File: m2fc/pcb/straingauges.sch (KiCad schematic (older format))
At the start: 29 parts

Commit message: update more bits on flight computer..
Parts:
- removed IC?: OP1177, 8MSOP, symbol OP1177
- removed IC? (x2): OP2177, symbol OP2177
- added IC?: AD8541, SC-70-5, symbol AD8541
- added IC? (x2): AD8656, SOIC8, symbol AD8656
- added TP? (x3): TESTPAD, symbol TESTPAD
- C?: value 1n -> 10n; footprint (none) -> 0603; Farnell (none) -> 2112704
- C? (x2): value C -> 8.2n; footprint (none) -> 0603; Farnell (none) -> 2210859
- C? (x2): value C -> 82n; footprint (none) -> 0603; Farnell (none) -> 1865539
- R?: Farnell 1160313 -> 2116614
- R?: value 10k -> 1k; Farnell 2332016 -> 2116678
- R?: value R -> 1.69k; footprint (none) -> 0603; Farnell (none) -> 2116702
- R?: value R -> 6.04k; footprint (none) -> 0603; Farnell (none) -> 2116761
- R?: value R -> 562; footprint (none) -> 0603; Farnell (none) -> 2117134
- R?: value R -> 17.8k; footprint (none) -> 0603; Farnell (none) -> 2117295
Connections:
- net labels added: VCC_2_REF
- wire segments 90 -> 102
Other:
- note added: "FILTERING\n==================\nSignals of interest: 0 to 1200Hz\nNyquist: 10kHz\nSample: 20kHz\n\nFRONTEND FILTER\n------------------\nFc = 1/(2 pi RC) = 16kHz\n\nANTIALIAS FILTER\n------------------\n-3dB: 2kHz\nRejection at Nyquist: -55dB"
- note added: "STRAIN GAUGES"
- note removed: "FILTERING\n===============\nSignals of interest: 0 to 1kHz\nNyquist: 5kHz\nSample: 10kHz\n\nFRONTEND FILTER\n------------------\nFc = 1/(2 pi RC) = 15915Hz\n\nANTIALIAS FILTER\n------------------\nFc = 2000Hz\nRejection at Nyquist:"
- moved on the sheet: C?, IC?, K?, R?

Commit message: everything... wired... up...
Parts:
- removed C? (x4): 10µ, 1411, symbol CP1
- removed C? (x4): 100n, 0603, symbol C
- removed C?: 10n, 0603, symbol C
- removed C? (x2): 8.2n, 0603, symbol C
- removed C? (x2): 82n, 0603, symbol C
- removed IC?: AD8226, 8MSOP, symbol AD8226
- removed IC?: AD8541, SC-70-5, symbol AD8541
- removed IC? (x2): AD8656, SOIC8, symbol AD8656
- removed K?: CONN_3, symbol CONN_3
- removed R?: 249, 0603, symbol R
- removed R? (x2): 10k, 0603, symbol R
- removed R? (x3): 120, 0603, symbol R
- removed R?: 1k, 0603, symbol R
- removed R?: 1.69k, 0603, symbol R
- removed R?: 6.04k, 0603, symbol R
- removed R?: 562, 0603, symbol R
- removed R?: 17.8k, 0603, symbol R
- removed TP? (x3): TESTPAD, symbol TESTPAD
- added C? (x12): 100n, 0603, symbol C
- added C? (x12): 10µ, 1411, symbol CP1
- added C? (x3): 10n, 0603, symbol C
- added C? (x6): 8.2n, 0603, symbol C
- added C? (x6): 82n, 0603, symbol C
- added IC? (x3): AD8226, 8MSOP, symbol AD8226
- added IC? (x3): AD8541, SC-70-5, symbol AD8541
- added IC? (x6): AD8656, SOIC8, symbol AD8656
- added K? (x3): CONN_3, symbol CONN_3
- added R? (x6): 10k 0.1%, 0603, symbol R
- added R? (x3): 249, 0603, symbol R
- added R? (x3): 1k, 0603, symbol R
- added R? (x3): 1.69k, 0603, symbol R
- added R? (x3): 6.04k, 0603, symbol R
- added R? (x3): 562, 0603, symbol R
- added R? (x3): 17.8k, 0603, symbol R
- added TP? (x3): TESTPAD, symbol TESTPAD
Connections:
- net labels added: STRAIN_2, STRAIN_3
- net labels removed: VCC_2_REF
- wire segments 102 -> 225
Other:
- note added: "STRAIN GAUGE 2"
- note added: "STRAIN GAUGE 3"

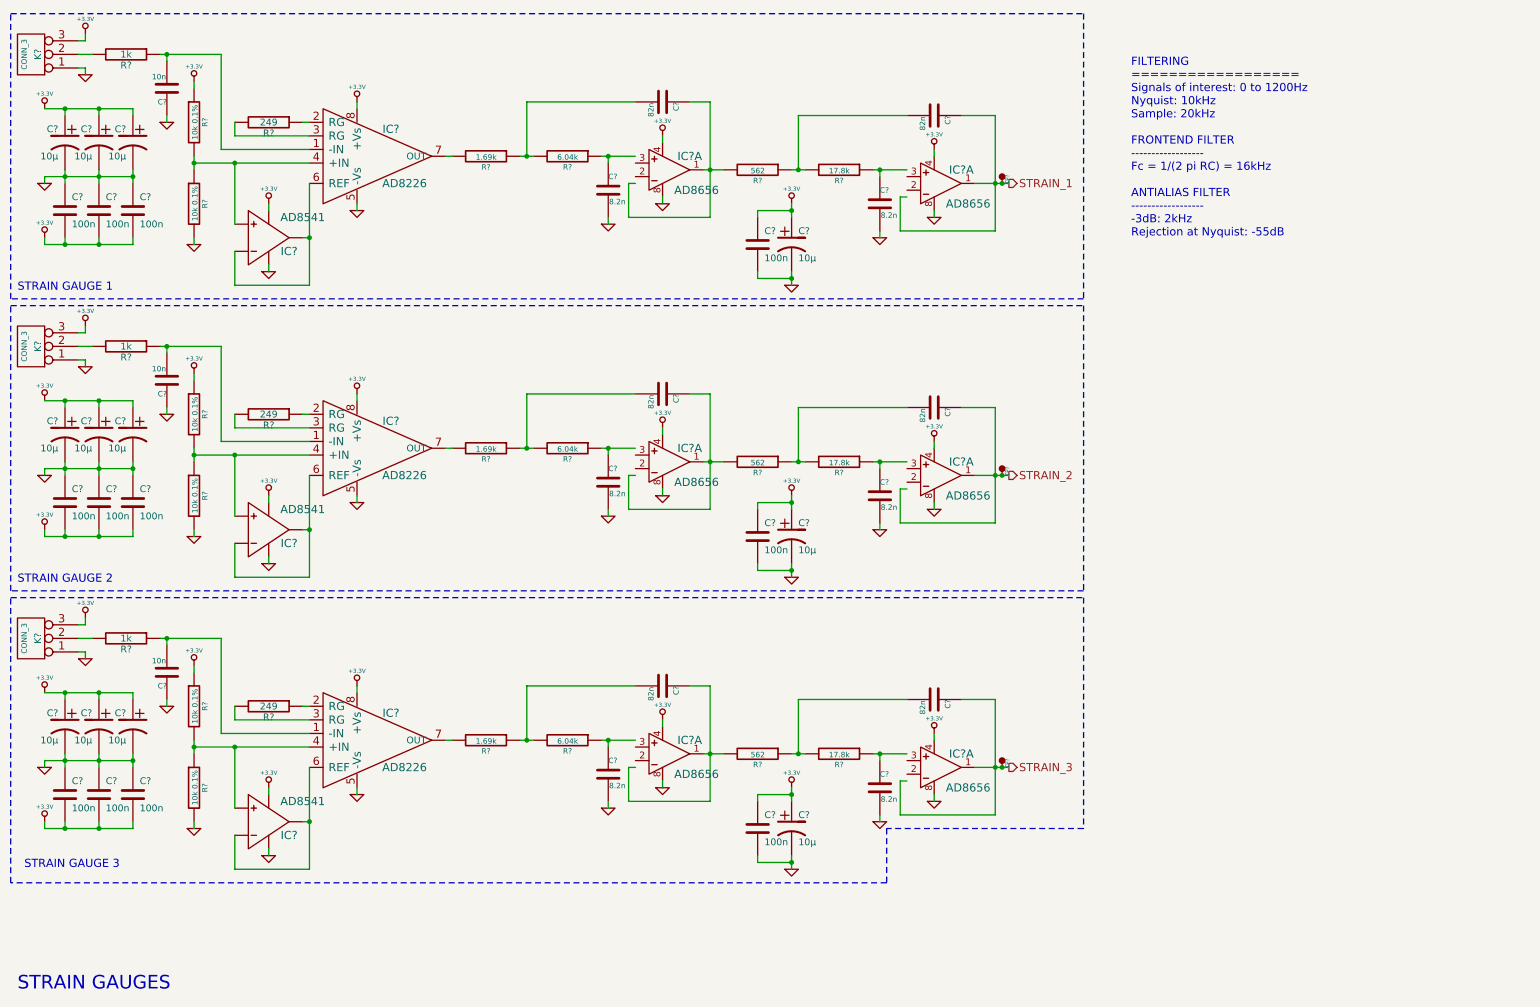
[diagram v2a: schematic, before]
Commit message: fix all the erc errors
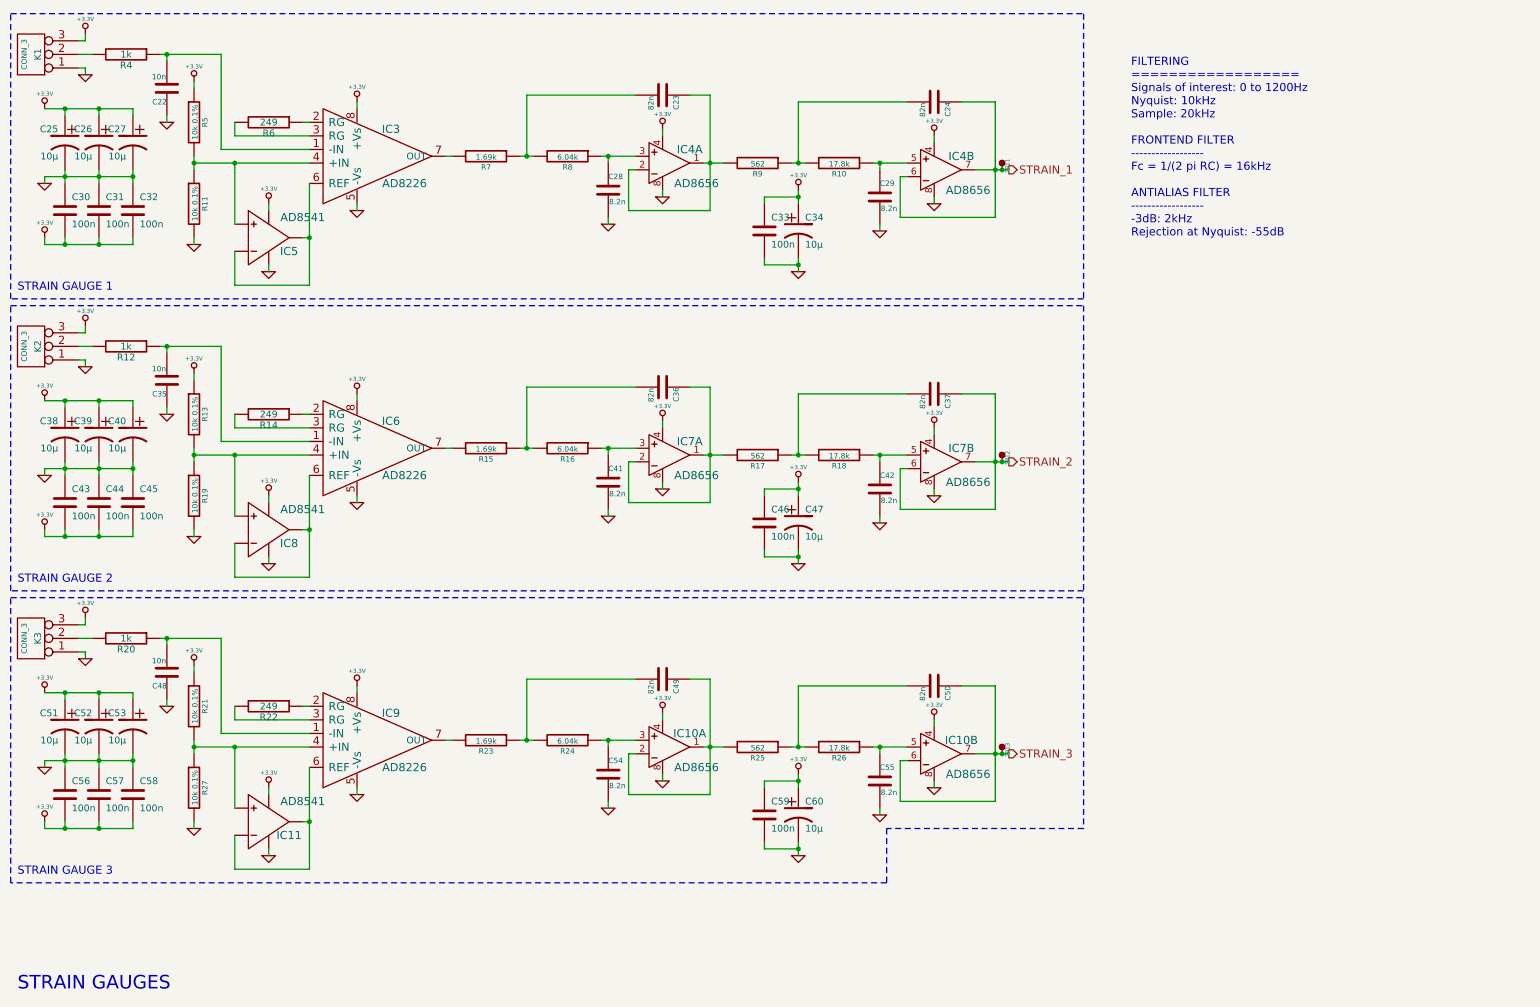
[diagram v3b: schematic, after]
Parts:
- removed C? (x8): 100n, 0603, symbol C
- removed C? (x8): 10µ, 1411, symbol CP1
- removed C? (x2): 10n, 0603, symbol C
- removed C? (x4): 8.2n, 0603, symbol C
- removed C? (x4): 82n, 0603, symbol C
- removed IC? (x2): AD8226, 8MSOP, symbol AD8226
- removed IC? (x2): AD8541, SC-70-5, symbol AD8541
- removed IC? (x4): AD8656, SOIC8, symbol AD8656
- removed K? (x2): CONN_3, symbol CONN_3
- removed R? (x4): 10k 0.1%, 0603, symbol R
- removed R? (x2): 249, 0603, symbol R
- removed R? (x2): 1k, 0603, symbol R
- removed R? (x2): 1.69k, 0603, symbol R
- removed R? (x2): 6.04k, 0603, symbol R
- removed R? (x2): 562, 0603, symbol R
- removed R? (x2): 17.8k, 0603, symbol R
- removed TP? (x2): TESTPAD, symbol TESTPAD
- added C35, C48: 10n, 0603, symbol C
- added C36, C37, C49, C50: 82n, 0603, symbol C
- added C38, C39, C40, C47, C51, C52, C53, C60: 10µ, 1411, symbol CP1
- added C41, C42, C54, C55: 8.2n, 0603, symbol C
- added C43, C44, C45, C46, C56, C57, C58, C59: 100n, 0603, symbol C
- added IC10, IC7: AD8656, SOIC8, symbol AD8656
- added IC11, IC8: AD8541, SC-70-5, symbol AD8541
- added IC6, IC9: AD8226, 8MSOP, symbol AD8226
- added K2, K3: CONN_3, symbol CONN_3
- added R12, R20: 1k, 0603, symbol R
- added R13, R19, R21, R27: 10k 0.1%, 0603, symbol R
- added R14, R22: 249, 0603, symbol R
- added R15, R23: 1.69k, 0603, symbol R
- added R16, R24: 6.04k, 0603, symbol R
- added R17, R25: 562, 0603, symbol R
- added R18, R26: 17.8k, 0603, symbol R
- added TP12, TP13: TESTPAD, symbol TESTPAD
- gave numbers to parts that had none: 26
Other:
- moved on the sheet: C23, C24, C29, C33, C34, IC4A, R10, R9, TP11

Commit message: further wibbling about things
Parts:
- R14, R22, R6: value 249 -> 330; Farnell 2116614 -> 1577599
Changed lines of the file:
@@
 P 2400 1300
 F 0 "R6" V 2480 1300 50  0000 C CNN
-F 1 "249" V 2400 1300 50  0000 C CNN
+F 1 "330" V 2400 1300 50  0000 C CNN
 F 2 "0603" H 2400 1300 60  0001 C CNN
 F 3 "" H 2400 1300 60  0001 C CNN
-F 4 "2116614" H 2400 1300 60  0001 C CNN "Farnell"
+F 4 "1577599" H 2400 1300 60  0001 C CNN "Farnell"
 	1    2400 1300
 	0    1    1    0
@@
 P 2400 3450
 F 0 "R14" V 2480 3450 50  0000 C CNN
-F 1 "249" V 2400 3450 50  0000 C CNN
+F 1 "330" V 2400 3450 50  0000 C CNN
 F 2 "0603" H 2400 3450 60  0001 C CNN
 F 3 "" H 2400 3450 60  0001 C CNN
-F 4 "2116614" H 2400 3450 60  0001 C CNN "Farnell"
+F 4 "1577599" H 2400 3450 60  0001 C CNN "Farnell"
 	1    2400 3450
 	0    1    1    0
@@
 P 2400 5600
 F 0 "R22" V 2480 5600 50  0000 C CNN
-F 1 "249" V 2400 5600 50  0000 C CNN
+F 1 "330" V 2400 5600 50  0000 C CNN
 F 2 "0603" H 2400 5600 60  0001 C CNN
 F 3 "" H 2400 5600 60  0001 C CNN
-F 4 "2116614" H 2400 5600 60  0001 C CNN "Farnell"
+F 4 "1577599" H 2400 5600 60  0001 C CNN "Farnell"
 	1    2400 5600
 	0    1    1    0

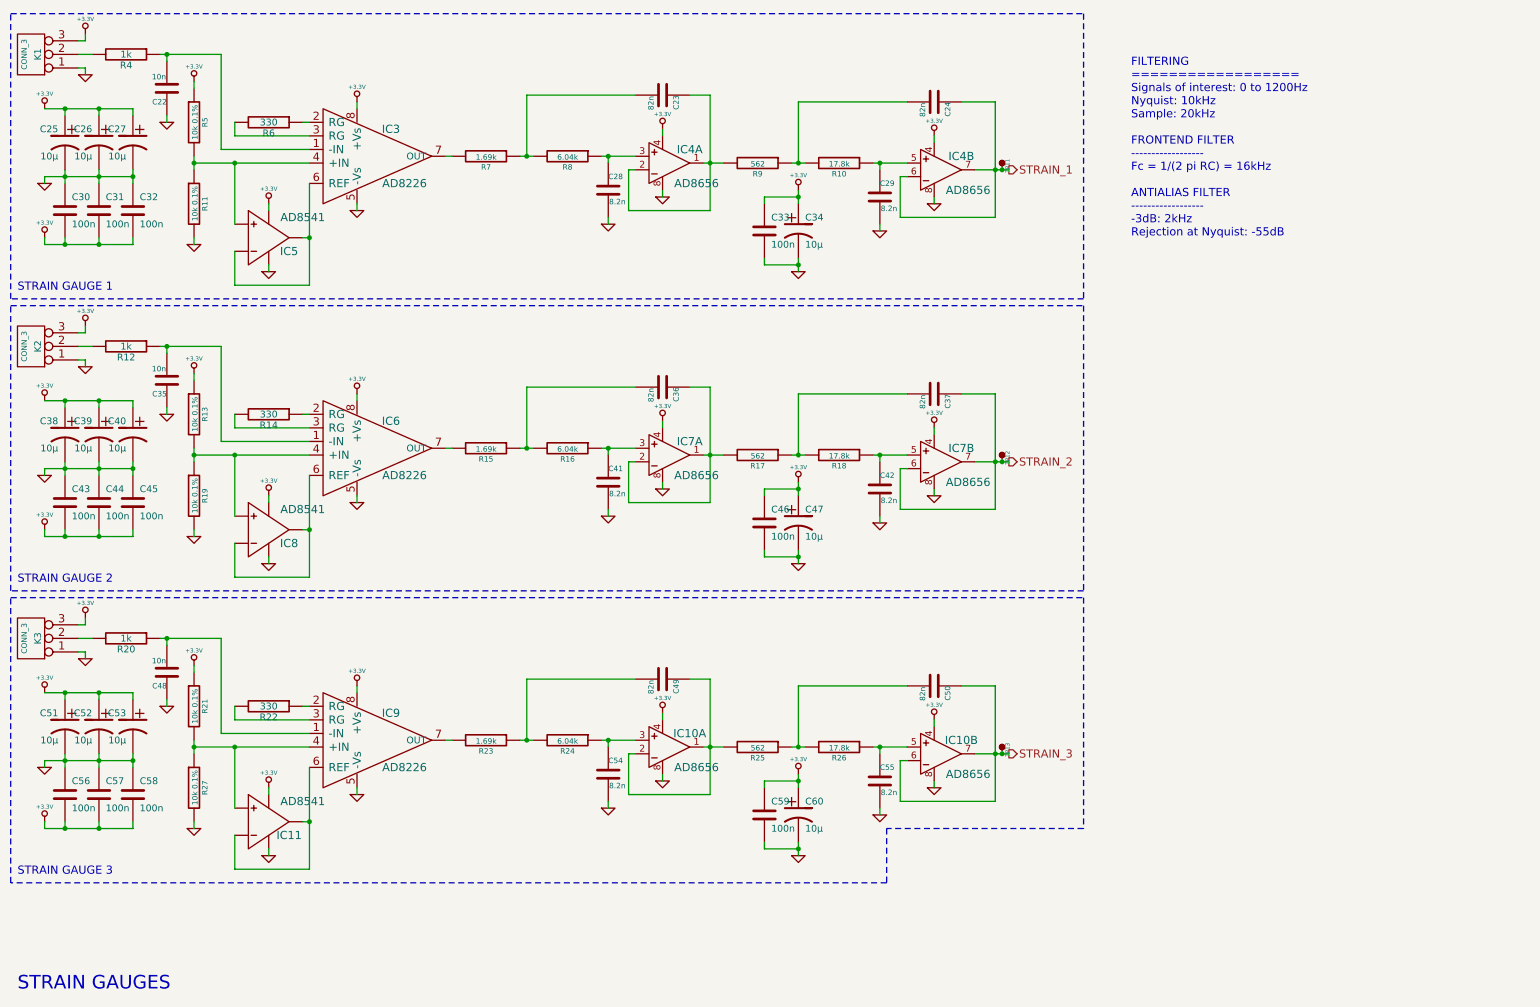
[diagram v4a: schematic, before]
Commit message: update m2fc sch with 3rd pyro and SJs
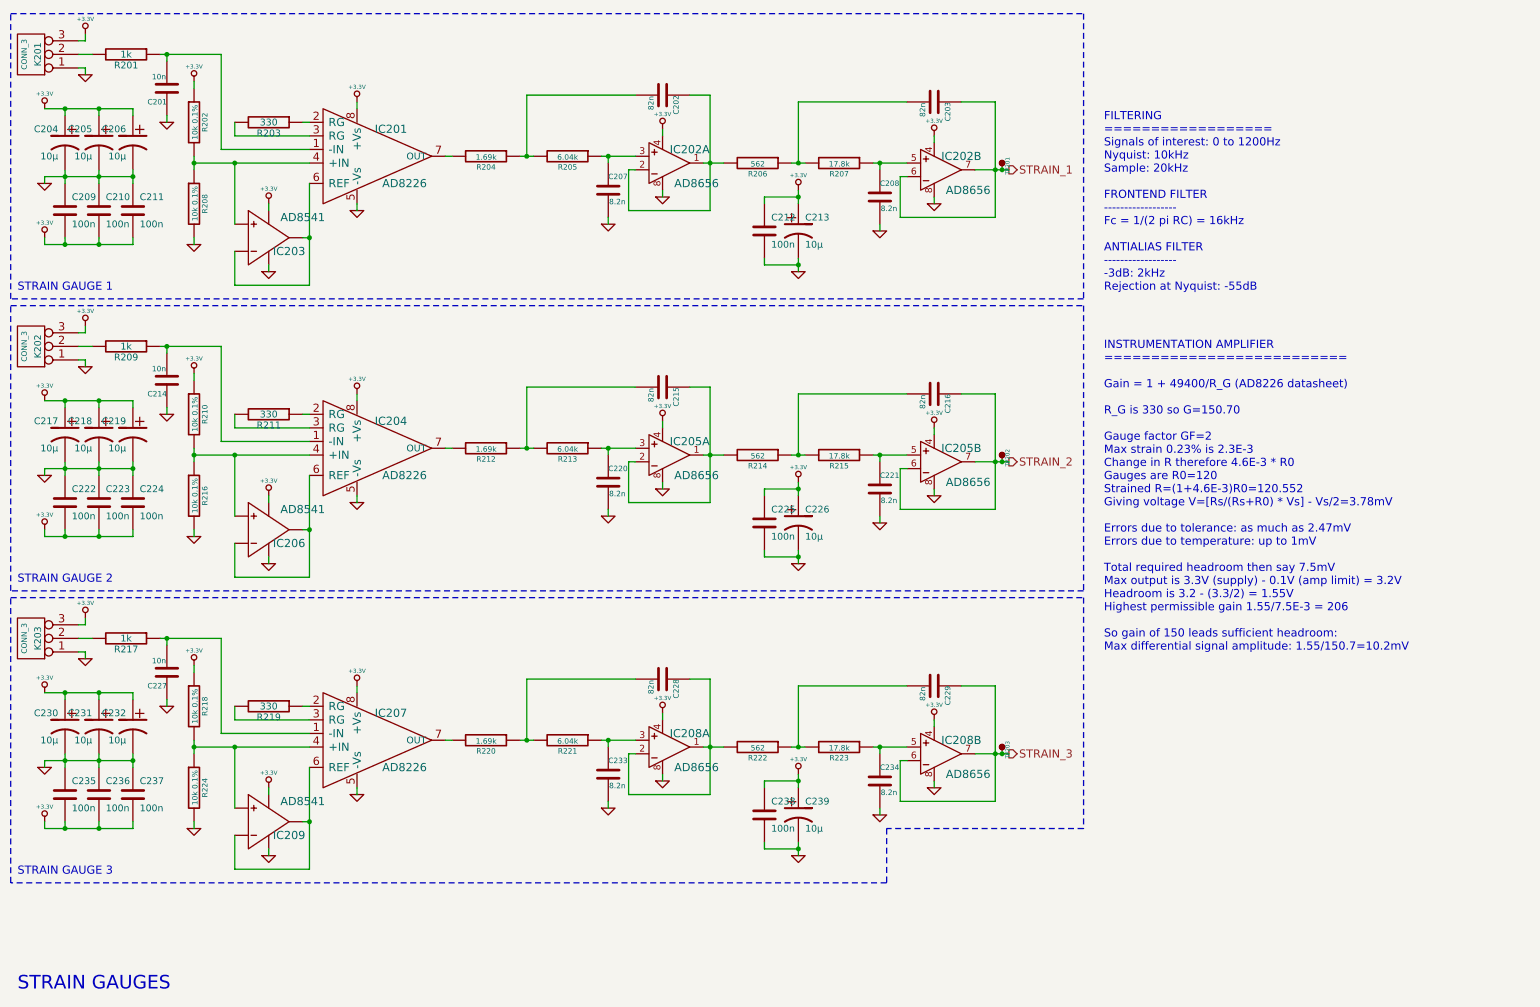
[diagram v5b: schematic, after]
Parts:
- renumbered C22 to C201, C23 to C202, C24 to C203, C25 to C204, C26 to C205, C27 to C206, C28 to C207, C29 to C208, C30 to C209, C31 to C210, C32 to C211, C33 to C212, C34 to C213, C35 to C214, C36 to C215, C37 to C216, C38 to C217, C39 to C218, C40 to C219, C41 to C220, C42 to C221, C43 to C222, C44 to C223, C45 to C224, C46 to C225, C47 to C226, C48 to C227, C49 to C228, C50 to C229, C51 to C230, C52 to C231, C53 to C232, C54 to C233, C55 to C234, C56 to C235, C57 to C236, C58 to C237, C59 to C238, C60 to C239, IC3 to IC201, IC4 to IC202, IC5 to IC203, IC6 to IC204, IC7 to IC205, IC8 to IC206, IC9 to IC207, IC10 to IC208, IC11 to IC209, K1 to K201, K2 to K202, K3 to K203, R4 to R201, R5 to R202, R6 to R203, R7 to R204, R8 to R205, R9 to R206, R10 to R207, R11 to R208, R12 to R209, R13 to R210, R14 to R211, R15 to R212, R16 to R213, R17 to R214, R18 to R215, R19 to R216, R20 to R217, R21 to R218, R22 to R219, R23 to R220, R24 to R221, R25 to R222, R26 to R223, R27 to R224, TP11 to TP201, TP12 to TP202, TP13 to TP203
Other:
- note added: "INSTRUMENTATION AMPLIFIER\n==========================\n\nGain = 1 + 49400/R_G (AD8226 datasheet)\n\nR_G is 330 so G=150.70\n\nGauge factor GF=2\nMax strain 0.23% is 2.3E-3\nChange in R therefore 4.6E-3 * R0\nGauges are R0=120\nStrained R=(1+4.6E-3)R0=120.552\nGiving voltage V=[Rs/(Rs+R0) * Vs] - Vs/2=3.78mV\n\nErrors due to tolerance: as much as 2.47mV\nErrors due to temperature: up to 1mV\n\nTot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"

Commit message: swap to JST PA range connectors
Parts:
- added U201, U202, U203: HOUSING, symbol PART
- K201, K202, K203: Farnell 1462950 -> 1830748
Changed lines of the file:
@@
 F 2 "" H 650 800 60  0000 C CNN
 F 3 "" H 650 800 60  0000 C CNN
-F 4 "1462950" H 650 800 60  0001 C CNN "Farnell"
+F 4 "1830748" H 650 800 60  0001 C CNN "Farnell"
 	1    650  800
 	-1   0    0    1
@@
 F 2 "" H 650 2950 60  0000 C CNN
 F 3 "" H 650 2950 60  0000 C CNN
-F 4 "1462950" H 650 2950 60  0001 C CNN "Farnell"
+F 4 "1830748" H 650 2950 60  0001 C CNN "Farnell"
 	1    650  2950
 	-1   0    0    1
@@
 F 2 "" H 650 5100 60  0000 C CNN
 F 3 "" H 650 5100 60  0000 C CNN
-F 4 "1462950" H 650 5100 60  0001 C CNN "Farnell"
+F 4 "1830748" H 650 5100 60  0001 C CNN "Farnell"
 	1    650  5100
 	-1   0    0    1
@@
 Text Notes 8550 5200 0    60   ~ 0
 INSTRUMENTATION AMPLIFIER\n==========================\n\nGain = 1 + 49400/R_G (AD8226 datasheet)\n\nR_G is 330 so G=150.70\n\nGauge factor GF=2\nMax strain 0.23% is 2.3E-3\nChange in R therefore 4.6E-3 * R0\nGauges are R0=120\nStrained R=(1+4.6E-3)R0=120.552\nGiving voltage V=[Rs/(Rs+R0) * Vs] - Vs/2=3.78mV\n\nErrors due to tolerance: as much as 2.47mV\nErrors due to temperature: up to 1mV\n\nTotal required headroom then say 7.5mV\nMax output is 3.3V (supply) - 0.1V (amp limit) = 3.2V\nHeadroom is 3.2 - (3.3/2) = 1.55V\nHighest permissible gain 1.55/7.5E-3 = 206\n\nSo gain of 150 leads sufficient headroom:\nMax differential signal amplitude: 1.55/150.7=10.2mV
+$Comp
+L PART U201
+U 1 1 53CEC561
+P 1300 650
+F 0 "U201" H 1350 650 60  0000 C CNN
+F 1 "HOUSING" H 1500 750 60  0000 C CNN
+F 2 "" H 1300 650 60  0000 C CNN
+F 3 "" H 1300 650 60  0000 C CNN
+F 4 "1830728" H 1300 650 60  0001 C CNN "Farnell"
+	1    1300 650
+	1    0    0    -1
+$EndComp
+$Comp
+L PART U202
+U 1 1 53CEC715
+P 1300 2800
+F 0 "U202" H 1350 2800 60  0000 C CNN
+F 1 "HOUSING" H 1500 2900 60  0000 C CNN
+F 2 "" H 1300 2800 60  0000 C CNN
+F 3 "" H 1300 2800 60  0000 C CNN
+F 4 "1830728" H 1300 2800 60  0001 C CNN "Farnell"
+	1    1300 2800
+	1    0    0    -1
+$EndComp
+$Comp
+L PART U203
+U 1 1 53CECA98
+P 1300 4950
+F 0 "U203" H 1350 4950 60  0000 C CNN
+F 1 "HOUSING" H 1500 5050 60  0000 C CNN
+F 2 "" H 1300 4950 60  0000 C CNN
+F 3 "" H 1300 4950 60  0000 C CNN
+F 4 "1830728" H 1300 4950 60  0001 C CNN "Farnell"
+	1    1300 4950
+	1    0    0    -1
+$EndComp
 $EndSCHEMATC

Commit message: rejig m2r schematic a little for i2c gps
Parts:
- IC201, IC204, IC207: footprint 8MSOP -> SOIC8; Farnell 1827359 -> 1827360
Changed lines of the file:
@@
 F 0 "IC201" H 3300 1750 60  0000 C CNN
 F 1 "AD8226" H 3400 1350 60  0000 C CNN
-F 2 "8MSOP" H 3050 1550 60  0001 C CNN
+F 2 "SOIC8" H 3050 1550 60  0001 C CNN
 F 3 "" H 3050 1550 60  0000 C CNN
-F 4 "1827359" H 3050 1550 60  0001 C CNN "Farnell"
+F 4 "1827360" H 3050 1550 60  0001 C CNN "Farnell"
 	1    3050 1550
 	1    0    0    -1
@@
 F 0 "IC204" H 3300 3900 60  0000 C CNN
 F 1 "AD8226" H 3400 3500 60  0000 C CNN
-F 2 "8MSOP" H 3050 3700 60  0001 C CNN
+F 2 "SOIC8" H 3050 3700 60  0001 C CNN
 F 3 "" H 3050 3700 60  0000 C CNN
-F 4 "1827359" H 3050 3700 60  0001 C CNN "Farnell"
+F 4 "1827360" H 3050 3700 60  0001 C CNN "Farnell"
 	1    3050 3700
 	1    0    0    -1
@@
 F 0 "IC207" H 3300 6050 60  0000 C CNN
 F 1 "AD8226" H 3400 5650 60  0000 C CNN
-F 2 "8MSOP" H 3050 5850 60  0001 C CNN
+F 2 "SOIC8" H 3050 5850 60  0001 C CNN
 F 3 "" H 3050 5850 60  0000 C CNN
-F 4 "1827359" H 3050 5850 60  0001 C CNN "Farnell"
+F 4 "1827360" H 3050 5850 60  0001 C CNN "Farnell"
 	1    3050 5850
 	1    0    0    -1

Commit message: quick go at wiring diagram
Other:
- note added: "SWAP TO 4PIN CONNECTORS\nTO ADD SHIELD CONNECTOR?"
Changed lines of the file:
@@
 	1    0    0    -1
 $EndComp
+Text Notes 2300 850  0    60   ~ 0
+SWAP TO 4PIN CONNECTORS\nTO ADD SHIELD CONNECTOR?
 $EndSCHEMATC
